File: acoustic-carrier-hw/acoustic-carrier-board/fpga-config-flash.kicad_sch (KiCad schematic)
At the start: 13 parts, among them IC1 ECP5-BGA256, J16 Conn_01x08_Socket, J6 Conn_01x10_Socket, U4 W25Q128JVS, U9 W25Q128JVS

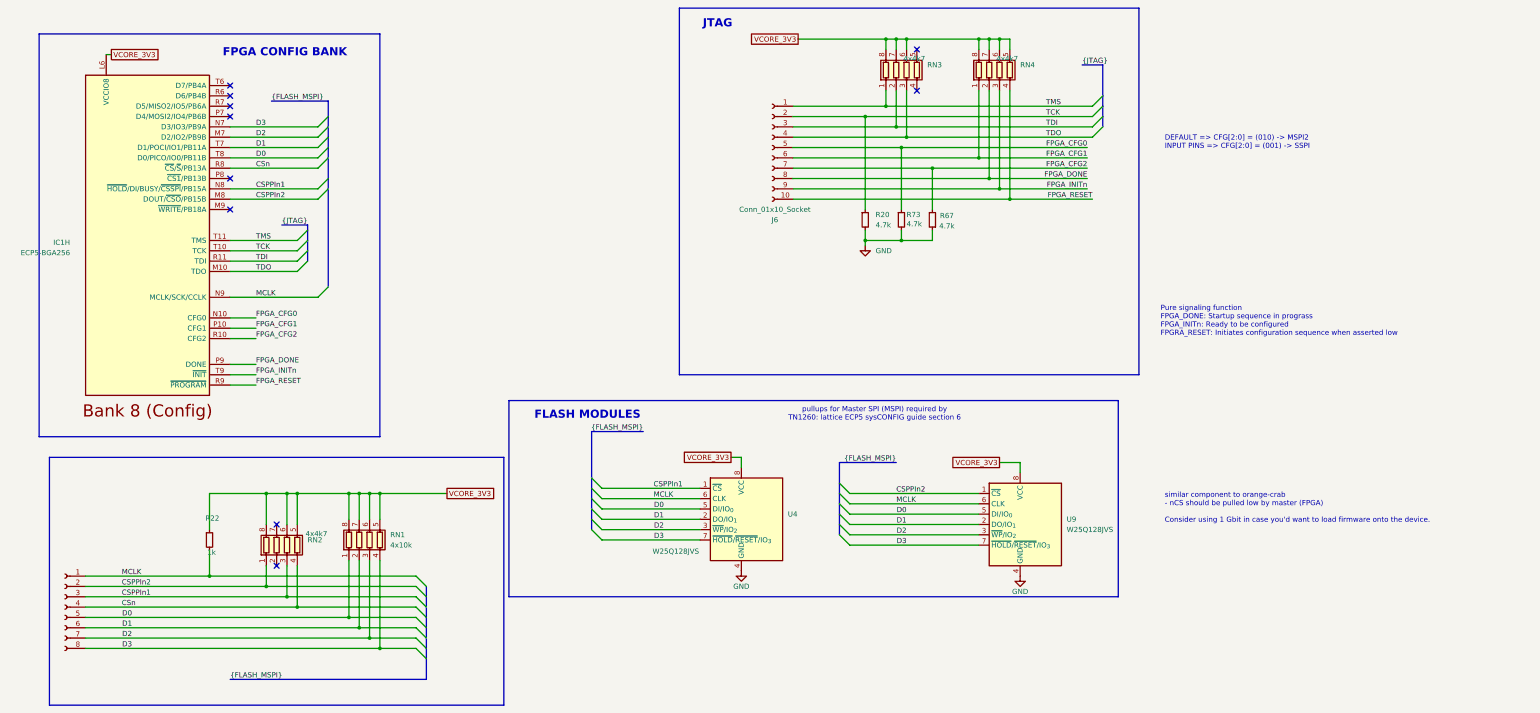
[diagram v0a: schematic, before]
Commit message: [carrier] Added hierarchical labels
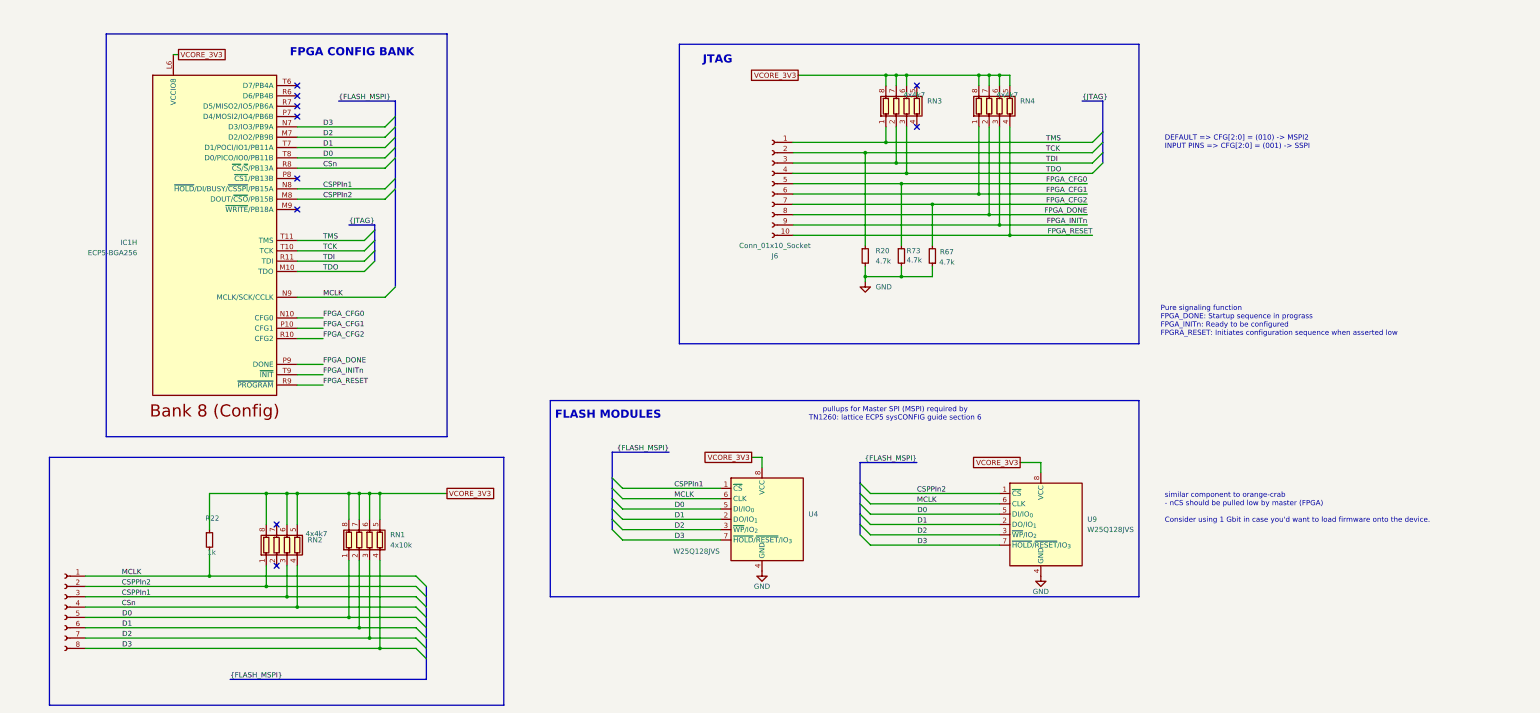
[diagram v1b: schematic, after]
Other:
- moved on the sheet: IC1H, J6, R20, R67, R73, RN3, RN4, U4, U9

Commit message: [carrier] Added decoupling caps to flash and comparators
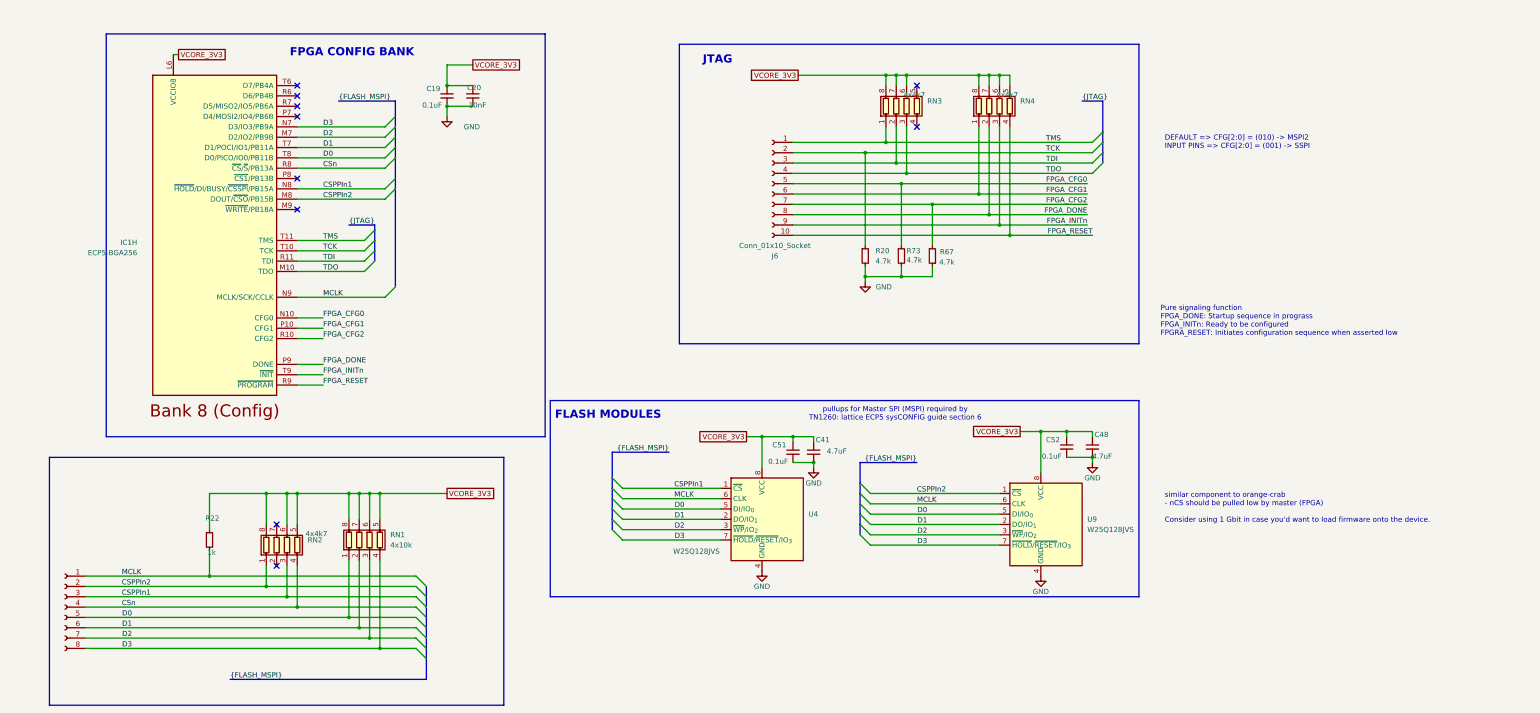
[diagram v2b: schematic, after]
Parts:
- added C19, C51, C52: 0.1uF, Capacitor_SMD:C_0402_1005Metric, symbol Device:C_Small
- added C20: 10nF, Capacitor_SMD:C_0402_1005Metric, symbol Device:C_Small
- added C41, C48: 4.7uF, Capacitor_SMD:C_0402_1005Metric, symbol Device:C_Small
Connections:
- net GND: now also C19.2, C20.2, C41.2, C48.2, C51.2, C52.2
- net VCORE_3V3: now also C19.1, C20.1, C41.1, C48.1, C51.1, C52.1

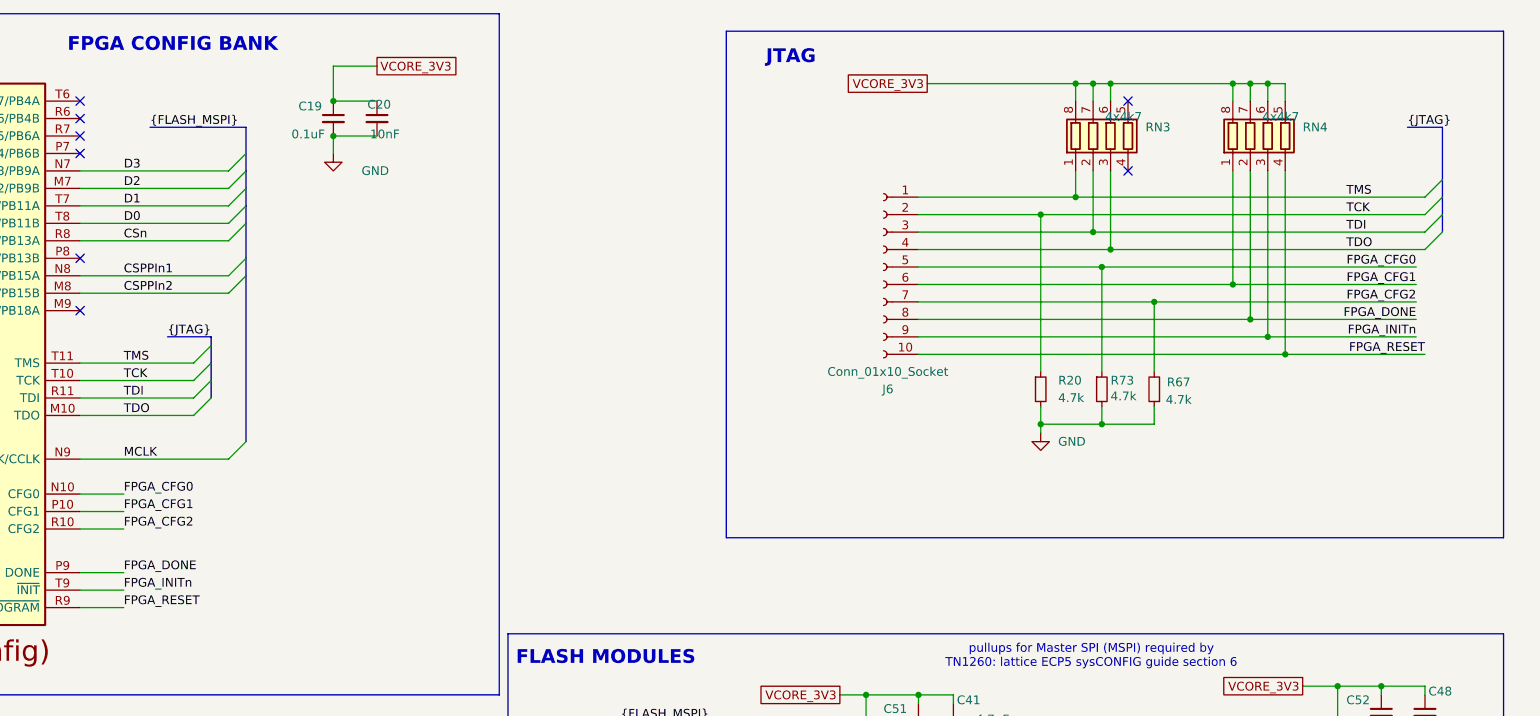
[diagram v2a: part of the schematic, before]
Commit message: [carrier] Added extra decoupling to ECP5U according to datasheet (next) perform page-wise checks, add testpoints
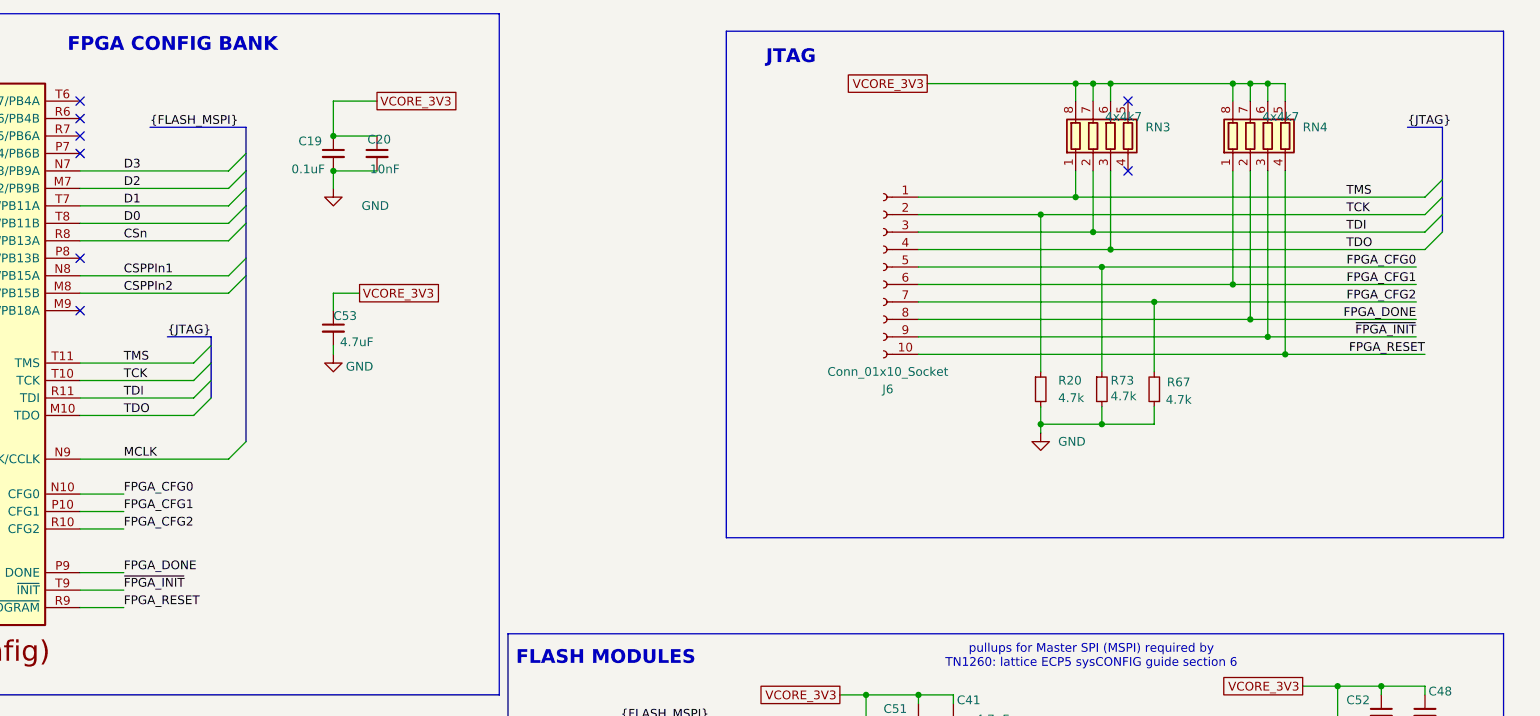
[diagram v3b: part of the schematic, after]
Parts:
- added C53: 4.7uF, Capacitor_SMD:C_0402_1005Metric, symbol Device:C_Small
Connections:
- net GND: now also C53.2
- net VCORE_3V3: now also C53.1
- net FPGA_INITn renamed ~{FPGA_INIT}
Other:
- moved on the sheet: C19, C20

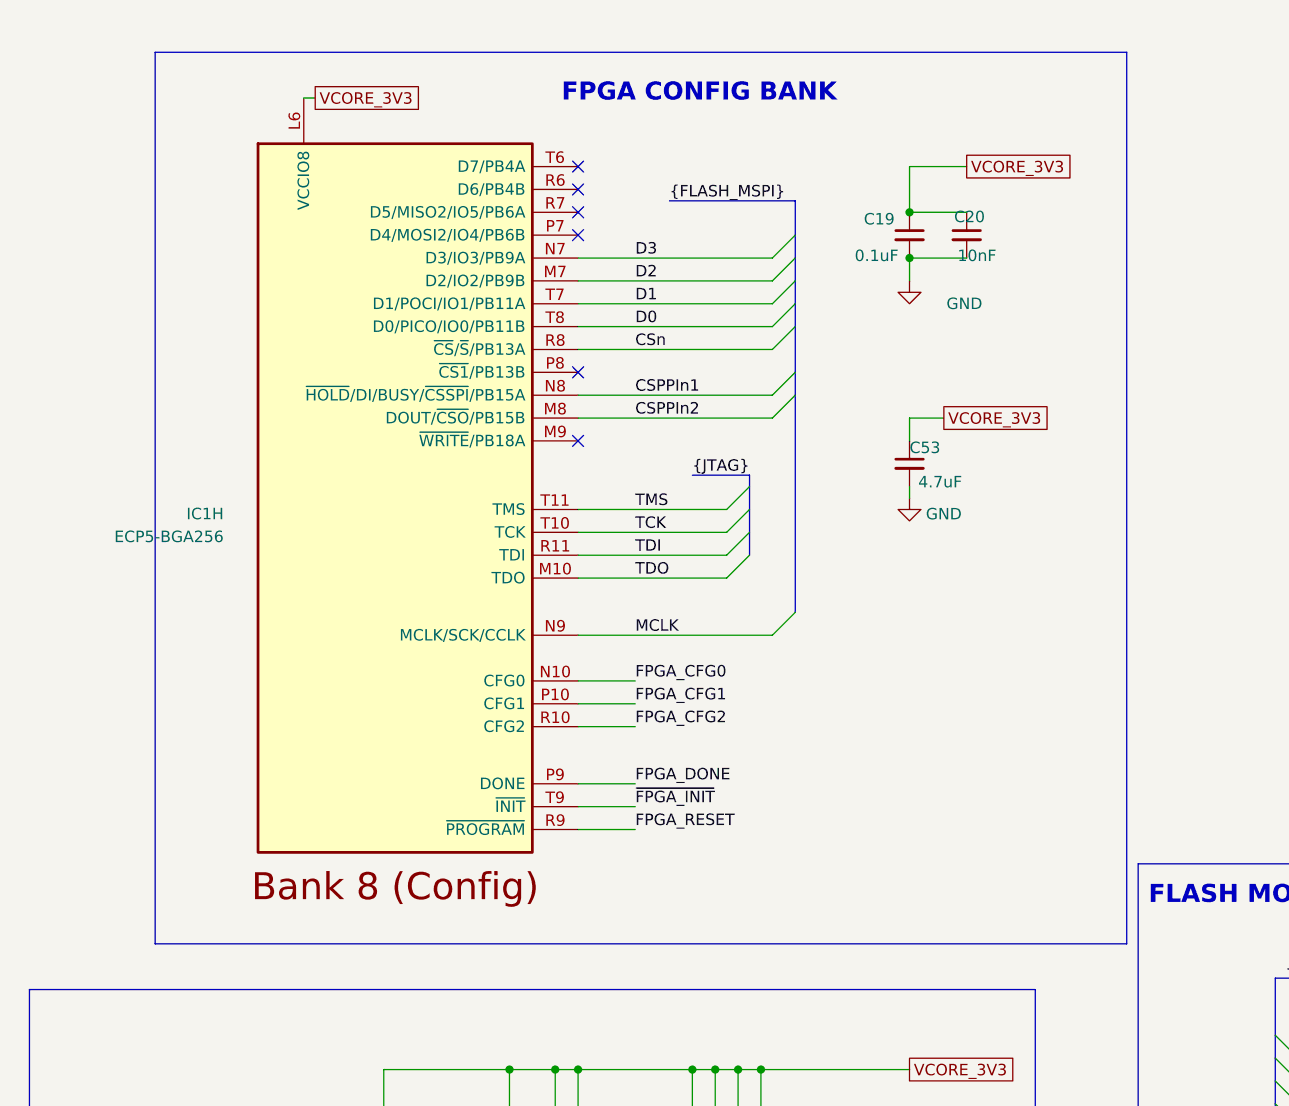
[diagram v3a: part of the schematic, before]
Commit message: [¢arrier] Finished checks, startting with layout and routing
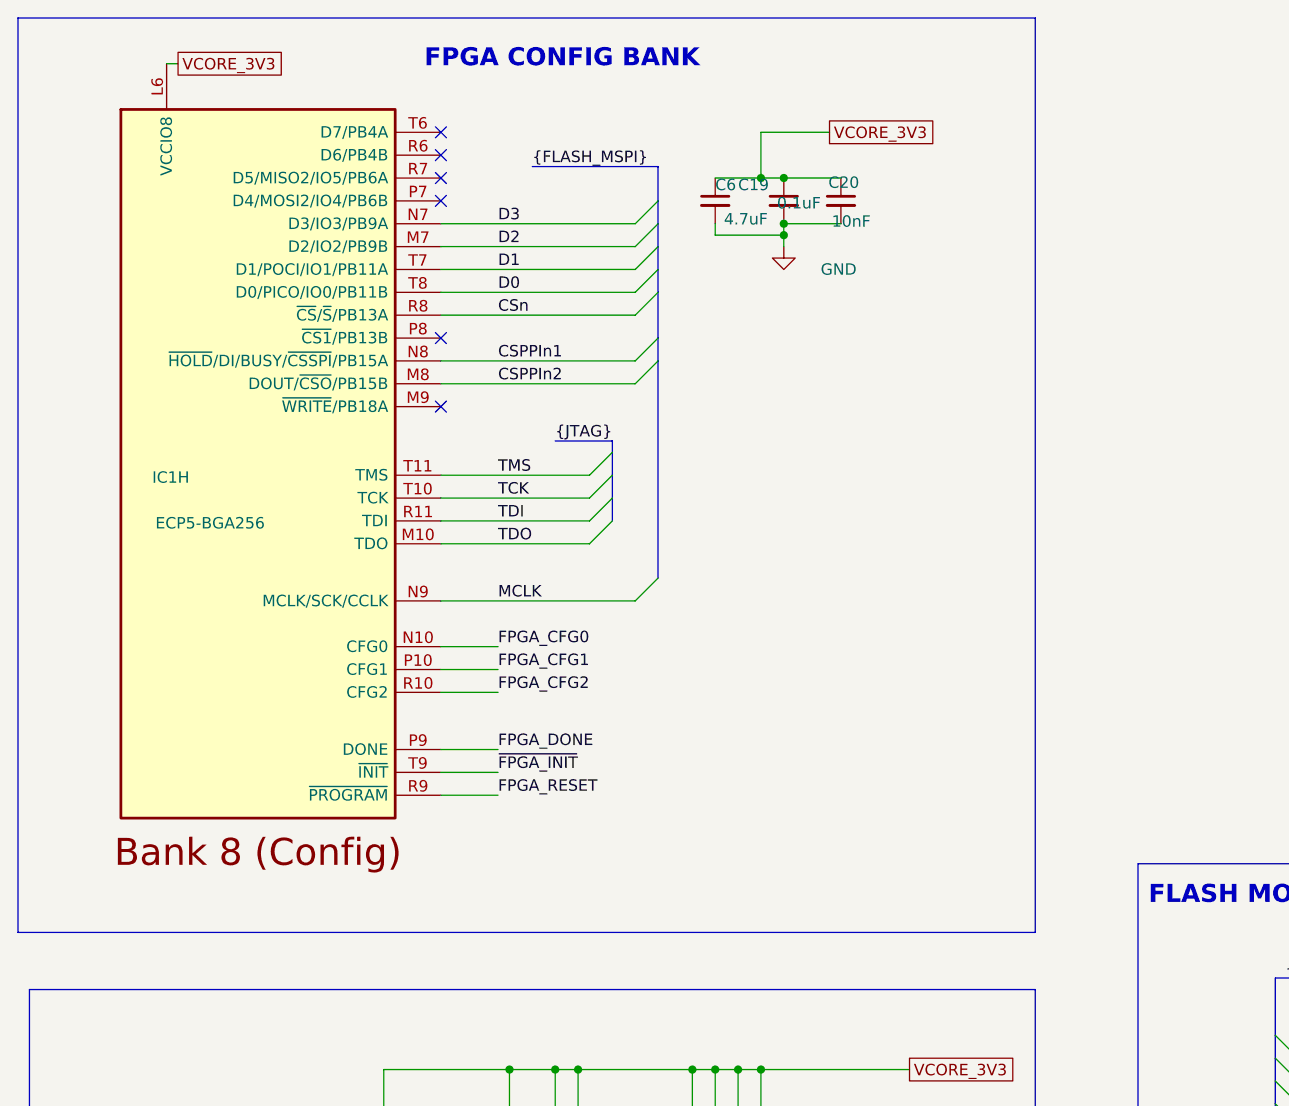
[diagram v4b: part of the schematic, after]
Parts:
- removed C53: 4.7uF, Capacitor_SMD:C_0402_1005Metric, symbol Device:C_Small
- added C6: 4.7uF, Capacitor_SMD:C_0402_1005Metric, symbol Device:C_Small
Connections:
- net GND: now also C6.2
- net VCORE_3V3: now also C6.1
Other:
- moved on the sheet: C19, C20, IC1H

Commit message: [¢arrier] Checked stackup theory, return current theory (next) continue researching ideal stackup
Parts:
- J16: footprint (none) -> Connector_PinSocket_2.54mm:PinSocket_1x08_P2.54mm_Horizontal
- J6: footprint (none) -> Connector_PinSocket_2.54mm:PinSocket_1x10_P2.54mm_Horizontal
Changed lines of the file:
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@@
 			)
 		)
-		(property "Footprint" ""
+		(property "Footprint" "Connector_PinSocket_2.54mm:PinSocket_1x10_P2.54mm_Horizontal"
 			(at 193.04 57.15 0)
 			(effects
@@
 			)
 		)
-		(property "Datasheet" "~"
+		(property "Datasheet" ""
 			(at 193.04 57.15 0)
 			(effects
@@
 			)
 		)
-		(property "Footprint" ""
+		(property "Footprint" "Connector_PinSocket_2.54mm:PinSocket_1x08_P2.54mm_Horizontal"
 			(at 19.05 161.29 0)
 			(effects
@@
 			)
 		)
-		(property "Datasheet" "~"
+		(property "Datasheet" ""
 			(at 19.05 161.29 0)
 			(effects
